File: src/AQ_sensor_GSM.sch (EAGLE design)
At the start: 64 parts, among them IC1 MIC29302WU, IC2 MCP73831/OT, J1 F-1X03-SIP-100-32, Q1 MMBT2222, SW1 PCM12SMTR, SW2 PCM12SMTR, U2 TEXAS_INSTRUMENTS_SN74HC125TE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, U3 TEXAS_INSTRUMENTS_LM1117IMP-3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, U4 EC200UCNAB-N05-SNNSA, X1 53048-08, X2 SIMLOCK-C707_10M006_512_2, X4 50 Ohms

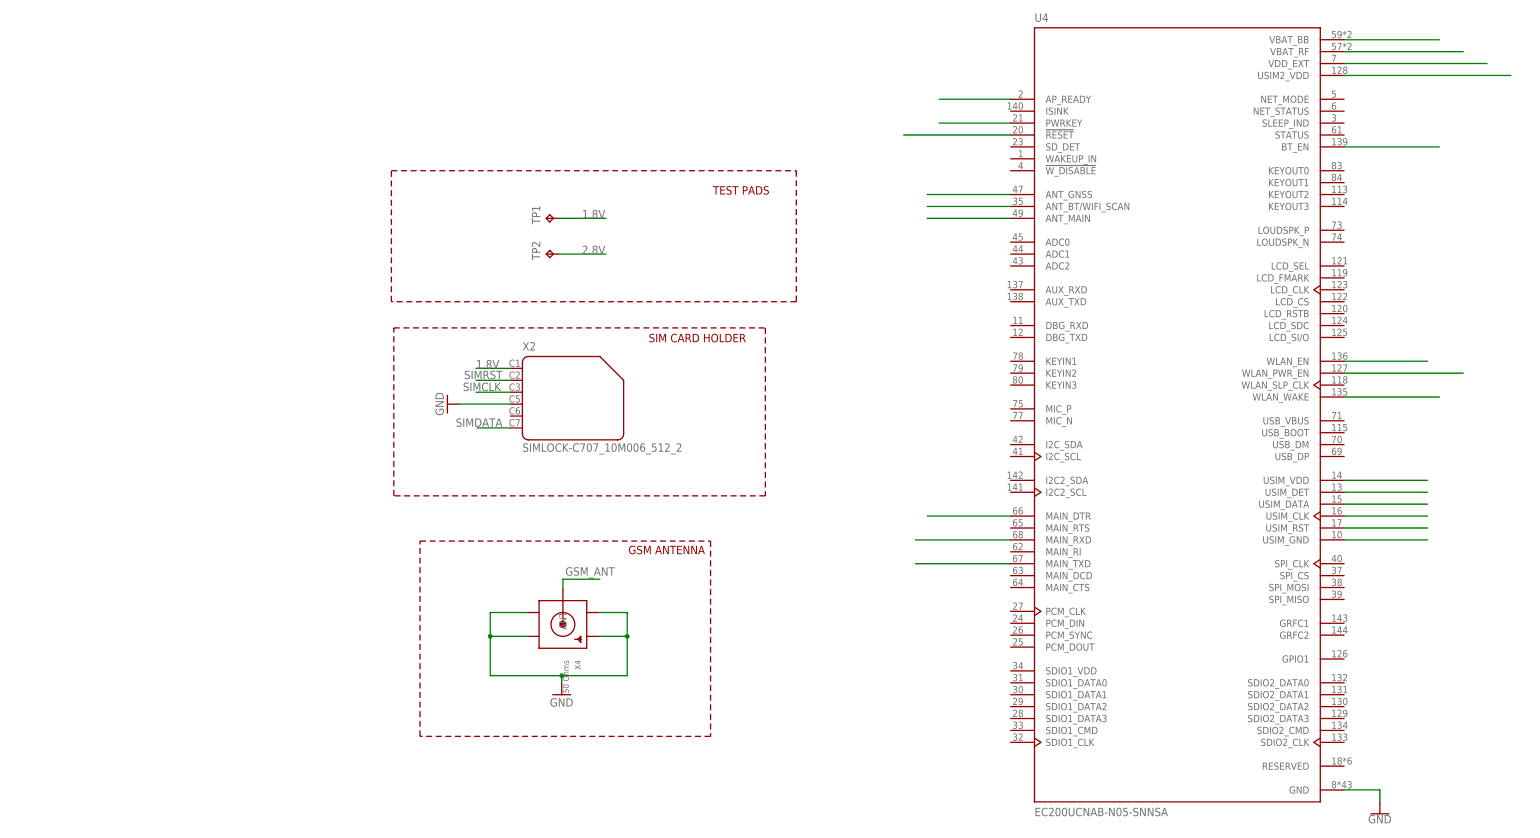
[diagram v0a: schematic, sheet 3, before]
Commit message: Added Nano sim adapter
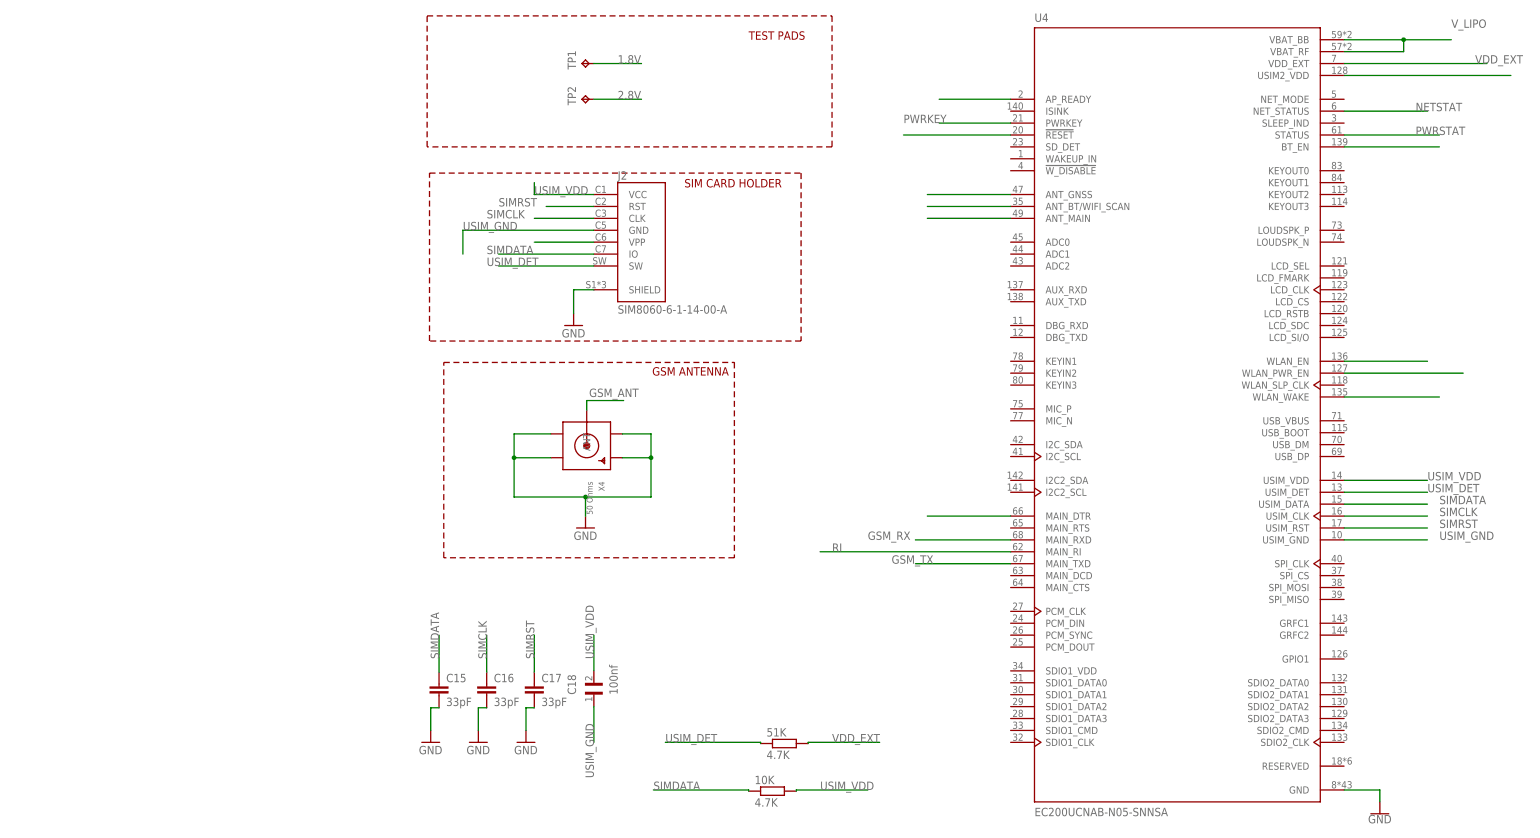
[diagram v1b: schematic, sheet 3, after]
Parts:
- removed X2: SIMLOCK-C707_10M006_512_2, AQ_sensor_GSM:SIMLOCK-C707_10M006_512_2
- added 10K, 51K: 4.7K, rcl:R-EU_R0603
- added C12: 470uf, T495X477K010ATE100:T495X477K010ATE100
- added C13, C18, C7: 100nf, 06035C104K4T2A:06035C104K4T2A
- added C14: EEEFT1E101AV, 100uf 25v capacitor:EEEFT1E101AV
- added C15, C16, C17: 33pF, rcl:C-EUC0603
- added D5: ESD56151W04, 4.7V TVS Diode:1N4148WS_RR
- added J2: SIM8060-6-1-14-00-A, Sim card nano XKNANO:SIM8060-6-1-14-00-A
- R11: value 470r -> 470R
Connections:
- removed net N$1: U4.VBAT_BB
- removed net N$17: U4.USIM_VDD
- removed net N$18: U4.USIM_DET
- removed net N$19: U4.USIM_DATA
- removed net N$2: U4.VBAT_RF
- removed net N$20: U4.USIM_CLK
- removed net N$21: U4.USIM_RST
- removed net N$22: U4.USIM_GND
- removed net N$24: U4.PWRKEY
- removed net N$31: U4.MAIN_TXD
- removed net N$32: U4.MAIN_RXD
- new net USIM_DET: 51K.1, D3.5_CATHODE, J2.SW, U4.USIM_DET
- new net USIM_GND: C18.1, J2.GND, U4.USIM_GND
- new net USIM_VDD: 10K.2, C18.2, D3.1_CATHODE, J2.VCC, U4.USIM_VDD
- new net VDD_EXT: 51K.2, U4.VDD_EXT
- net 1.8V: no longer D3.1_CATHODE, X2.1
- net GND: now also C12.2, C13.1, C14.2, C15.2, C16.2, C17.2, C7.1, D5.A, J2.SHIELD; no longer X2.4
- net GSM_RX: now also U4.MAIN_RXD
- net GSM_TX: now also U4.MAIN_TXD
- net N$3: now also J2.VPP; no longer U4.VDD_EXT
- net N$34: now also C7.2, D5.K
- net NETSTAT: now also U4.NET_STATUS
- net PWRKEY: now also U4.PWRKEY
- net PWRSTAT: now also U4.STATUS
- net RI: now also U4.MAIN_RI
- net SIMCLK: now also C16.1, J2.CLK, U4.USIM_CLK; no longer X2.3
- net SIMDATA: now also 10K.1, C15.1, J2.IO, U4.USIM_DATA; no longer X2.6
- net SIMRST: now also C17.1, J2.RST, U4.USIM_RST; no longer X2.2
- net V_LIPO: now also C12.1, C13.2, C14.1, U4.VBAT_BB, U4.VBAT_RF
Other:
- moved on the sheet: TP1, TP2, X4

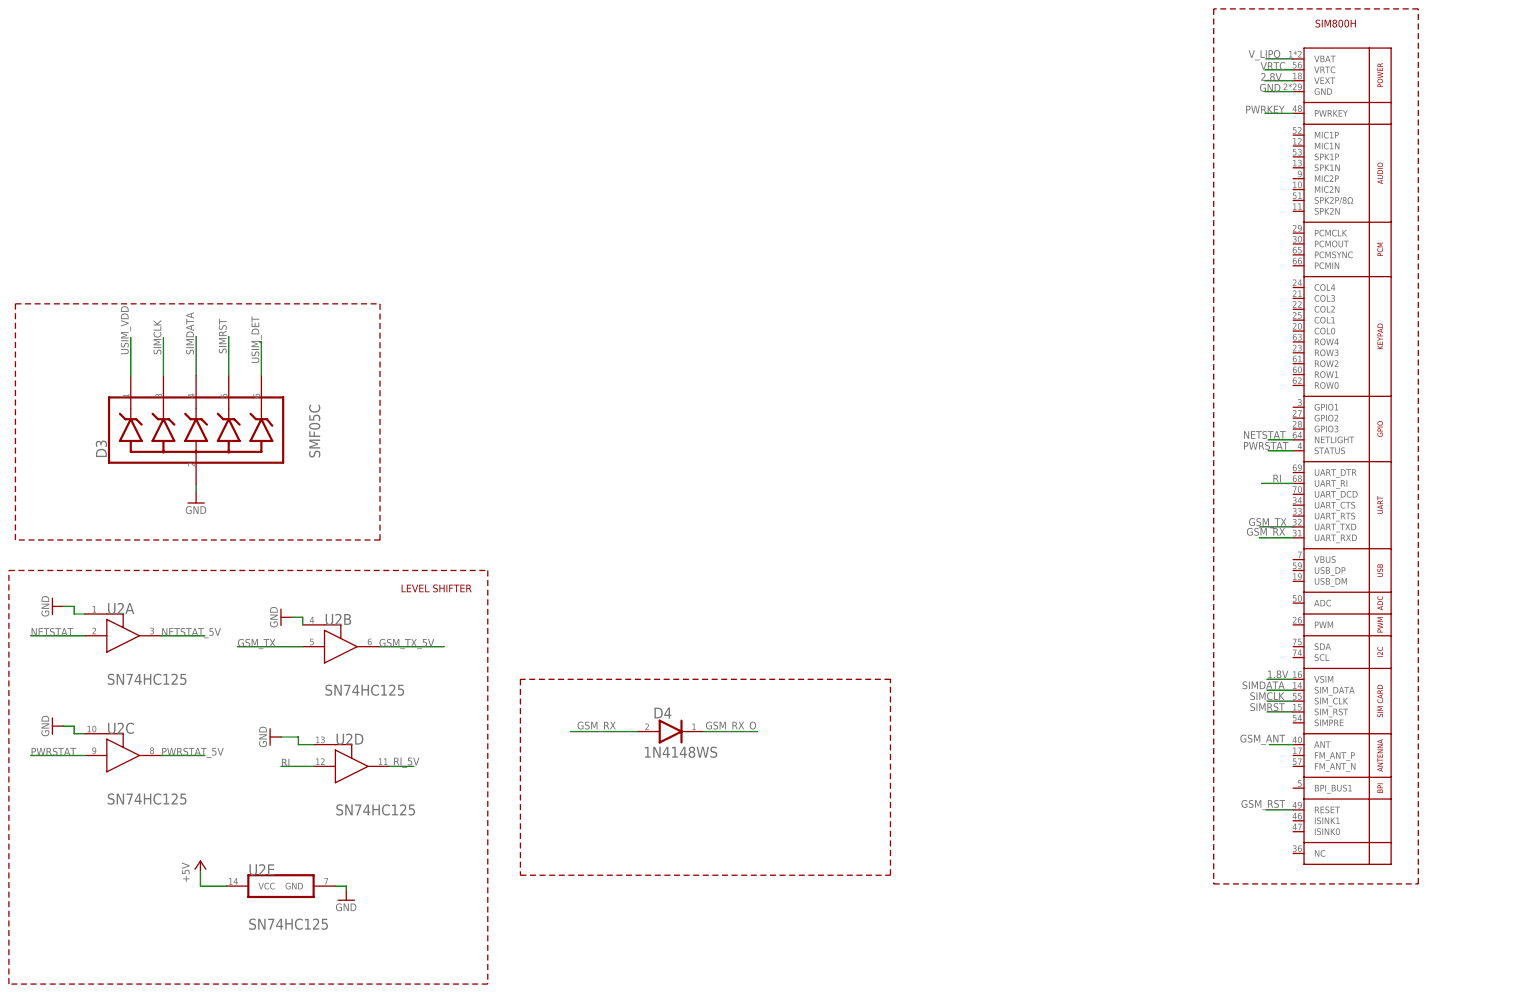
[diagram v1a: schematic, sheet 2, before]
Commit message: Added GNSS Antenna, reconfigured the PCB Layout
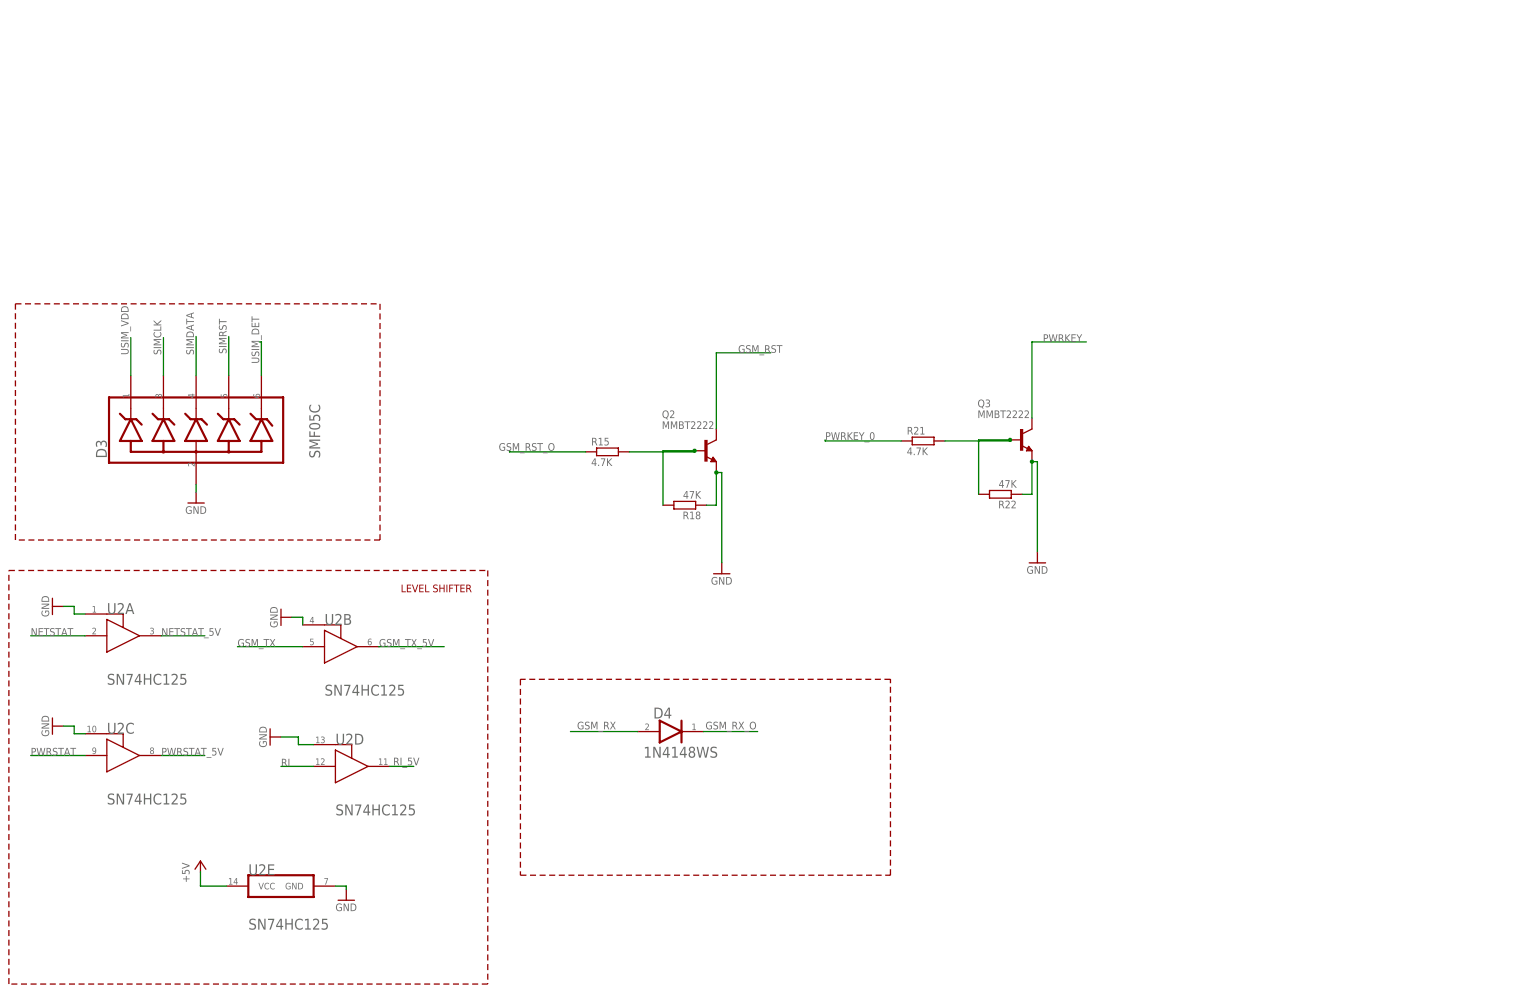
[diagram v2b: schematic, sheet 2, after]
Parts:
- removed SW2: PCM12SMTR, AQ_sensor_GSM:PCM12SMTR
- removed U1: (no value), AQ_sensor_GSM:GSM_SIM800L
- added ESP_RESET: KMR621NGLFS, AQ_sensor_GSM:KMR621NGLFS
- added GPS: 50 Ohms, AQ_sensor_GSM:SMACONNECTOR_EDGE_UFL
- added Q2, Q3: MMBT2222, MMBT2222_:MMBT2222
- added R15, R21: 4.7K, rcl:R-EU_R0603
- added R18, R22: 47K, rcl:R-EU_R0603
- renumbered S1 to GSM_RST, SW1 to POWER_SW, X4 to GSM
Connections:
- net N$29 renamed BT_ANT
- removed net N$26: U4.!RESET
- removed net N$28: U4.ANT_GNSS
- removed net N$30: U4.ANT_MAIN
- new net GNSS_ANT: GPS.ANT, U4.ANT_GNSS
- new net N$1: Q2.B, R15.2, R18.2
- new net N$18: SV2.8
- new net N$19: SV2.9
- new net N$2: Q3.B, R21.2, R22.2
- new net N$20: SV2.10
- new net N$21: SV2.11
- new net N$22: SV2.12
- new net PWRKEY_0: R21.1, SV1.15
- net +3V3: now also SV1.10
- net 1.8V: no longer U1.VSIM
- net 2.8V: no longer U1.VEXT
- net ESP_RST: now also ESP_RESET.2; no longer SW2.2
- net GND: now also ESP_RESET.1, GPS.GND1, GPS.GND2, GPS.GND3, GPS.GND4, Q2.E, Q3.E, R18.1, R22.1, SV1.9; no longer SW2.1, SW2.SHIELD, U1.GND
- net GSM_ANT: now also U4.ANT_MAIN; no longer U1.ANT
- net GSM_RST: now also Q2.C, U4.!RESET; no longer U1.RESET
- net GSM_RST_O: now also R15.1
- net GSM_RX: no longer U1.UART_RXD
- net GSM_TX: no longer U1.UART_TXD
- net NETSTAT: no longer U1.NETLIGHT
- net PWRKEY: now also Q3.C; no longer U1.PWRKEY
- net PWRSTAT: no longer U1.STATUS
- net RI: no longer U1.UART_RI
- net SIMCLK: no longer U1.SIM_CLK
- net SIMDATA: no longer U1.SIM_DATA
- net SIMRST: no longer U1.SIM_RST
- net VBAT_EN: now also SV2.7
- net VRTC: no longer U1.VRTC
- net V_LIPO: no longer U1.VBAT
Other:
- note added: "GNSS ANTENNA"
- note removed: "SIM800H"
- moved on the sheet: SV1, SV2

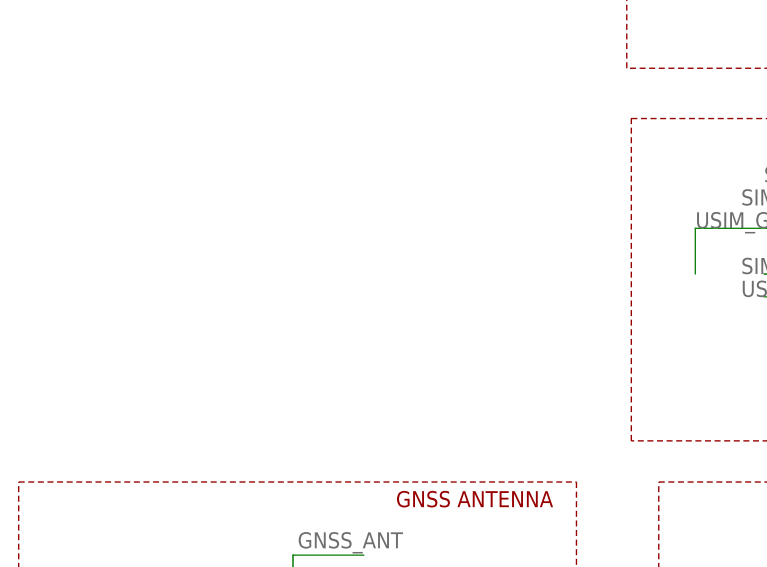
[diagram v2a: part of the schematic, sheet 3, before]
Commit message: Added Bluetooth and Wifi Antenna
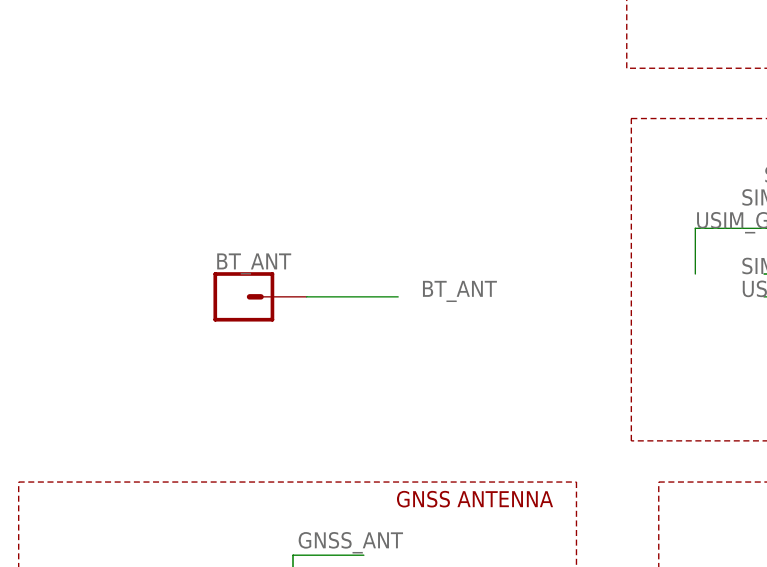
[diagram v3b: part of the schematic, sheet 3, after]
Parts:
- added BT_ANT: (no value), SparkFun-Connectors:CONN_01
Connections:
- net BT_ANT: now also BT_ANT.1
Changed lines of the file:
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@@
 <part name="GPS" library="AQ_sensor_GSM" library_urn="urn:adsk.eagle:library:30300195" deviceset="SMACONNECTOR" device="_EDGE_UFL" package3d_urn="urn:adsk.eagle:package:30300291/2" value="50 Ohms"/>
 <part name="GND12" library="supply1" library_urn="urn:adsk.eagle:library:371" deviceset="GND" device=""/>
+<part name="BT_ANT" library="SparkFun-Connectors" library_urn="urn:adsk.eagle:library:513" deviceset="CONN_01" device="" package3d_urn="urn:adsk.eagle:package:38028/1"/>
 </parts>
 <sheets>
@@
 <attribute name="VALUE" x="-174.498" y="137.16" size="1.778" layer="96"/>
 </instance>
+<instance part="BT_ANT" gate="G$1" x="-177.8" y="195.58" smashed="yes">
+<attribute name="VALUE" x="-180.34" y="190.754" size="1.778" layer="96" font="vector"/>
+<attribute name="NAME" x="-180.34" y="198.628" size="1.778" layer="95" font="vector"/>
+</instance>
 </instances>
 <busses>
@@
 <label x="-30.48" y="208.28" size="1.778" layer="95"/>
 </segment>
-</net>
+<segment>
+<pinref part="BT_ANT" gate="G$1" pin="1"/>
+<wire x1="-170.18" y1="195.58" x2="-160.02" y2="195.58" width="0.1524" layer="91"/>
+<label x="-157.48" y="195.58" size="1.778" layer="95"/>
+</segment>
+</net>
